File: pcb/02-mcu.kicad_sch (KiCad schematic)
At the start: 0 parts

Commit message: Setup project structure with organised sub-sheets
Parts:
- added U1: STM32G474RET6, Package_QFP:LQFP-64_10x10mm_P0.5mm, symbol MCU_ST_STM32G4:STM32G474RETx
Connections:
- new net: U1.15 (VSS), U1.31 (VSS), U1.47 (VSS), U1.63 (VSS)
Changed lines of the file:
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@@
 	(generator_version "10.0")
 	(paper "A4")
+	(symbol
+		(lib_id "MCU_ST_STM32G4:STM32G474RETx")
+		(at 59.69 71.12 0)
+		(unit 1)
+		(body_style 1)
+		(exclude_from_sim no)
+		(in_bom yes)
+		(on_board yes)
+		(in_pos_files yes)
+		(dnp no)
+		(fields_autoplaced yes)
+		(property "Reference" "U1"
+			(at 64.3733 119.38 0)
+			(show_name no)
+			(do_not_autoplace no)
+			(effects
+				(font
+					(size 1.27 1.27)
+				)
+				(justify left)
+			)
+		)
+		(property "Value" "STM32G474RET6"
+			(at 64.3733 121.92 0)
+			(show_name no)
+			(do_not_autoplace no)
+			(effects
+				(font
+					(size 1.27 1.27)
+				)
+				(justify left)
+			)
+		)
+		(property "Footprint" "Package_QFP:LQFP-64_10x10mm_P0.5mm"
+			(at 44.45 116.84 0)
+			(hide yes)
+			(show_name no)
+			(do_not_autoplace no)
+			(effects
+				(font
+					(size 1.27 1.27)
+				)
+				(justify right)
+			)
+		)
+		(property "Datasheet" "https://www.st.com/resource/en/datasheet/stm32g474re.pdf"
+			(at 59.69 71.12 0)
+			(hide yes)
+			(show_name no)
+			(do_not_autoplace no)
+			(effects
+				(font
+					(size 1.27 1.27)
+				)
+			)
+		)
+		(property "Description" "STMicroelectronics Arm Cortex-M4 MCU, 512KB flash, 128KB RAM, 170 MHz, 1.71-3.6V, 52 GPIO, LQFP64"
+			(at 59.69 71.12 0)
+			(hide yes)
+			(show_name no)
+			(do_not_autoplace no)
+			(effects
+				(font
+					(size 1.27 1.27)
+				)
+			)
+		)
+		(property "LCSC Part No" ""
+			(at 59.69 71.12 0)
+			(hide yes)
+			(show_name no)
+			(do_not_autoplace no)
+			(effects
+				(font
+					(size 1.27 1.27)
+				)
+			)
+		)
+		(property "Notes" ""
+			(at 59.69 71.12 0)
+			(hide yes)
+			(show_name no)
+			(do_not_autoplace no)
+			(effects
+				(font
+					(size 1.27 1.27)
+				)
+			)
+		)
+		(pin "40"
+		)
+		(pin "34"
+		)
+		(pin "36"
+		)
+		(pin "37"
+		)
+		(pin "38"
+		)
+		(pin "39"
+		)
+		(pin "35"
+		)
+		(pin "28"
+		)
+		(pin "30"
+		)
+		(pin "31"
+		)
+		(pin "32"
+		)
+		(pin "33"
+		)
+		(pin "29"
+		)
+		(pin "45"
+		)
+		(pin "46"
+		)
+		(pin "44"
+		)
+		(pin "47"
+		)
+		(pin "43"
+		)
+		(pin "48"
+		)
+		(pin "49"
+		)
+		(pin "42"
+		)
+		(pin "41"
+		)
+		(pin "1"
+		)
+		(pin "20"
+		)
+		(pin "19"
+		)
+		(pin "18"
+		)
+		(pin "17"
+		)
+		(pin "16"
+		)
+		(pin "15"
+		)
+		(pin "14"
+		)
+		(pin "13"
+		)
+		(pin "12"
+		)
+		(pin "11"
+		)
+		(pin "10"
+		)
+		(pin "9"
+		)
+		(pin "8"
+		)
+		(pin "7"
+		)
+		(pin "6"
+		)
+		(pin "5"
+		)
+		(pin "4"
+		)
+		(pin "3"
+		)
+		(pin "2"
+		)
+		(pin "50"
+		)
+		(pin "51"
+		)
+		(pin "52"
+		)
+		(pin "53"
+		)
+		(pin "54"
+		)
+		(pin "55"
+		)
+		(pin "56"
+		)
+		(pin "57"
+		)
+		(pin "58"
+		)
+		(pin "59"
+		)
+		(pin "60"
+		)
+		(pin "61"
+		)
+		(pin "62"
+		)
+		(pin "63"
+		)
+		(pin "64"
+		)
+		(pin "21"
+		)
+		(pin "27"
+		)
+		(pin "26"
+		)
+		(pin "25"
+		)
+		(pin "23"
+		)
+		(pin "22"
+		)
+		(pin "24"
+		)
+		(instances
+			(project "FluxNode-FOC"
+				(path "/c3755418-04f3-4b36-86ed-bd05a53b8f5f/2366da82-dc31-4919-b23c-1b211a77679f"
+					(reference "U1")
+					(unit 1)
+				)
+			)
+		)
+	)
 )

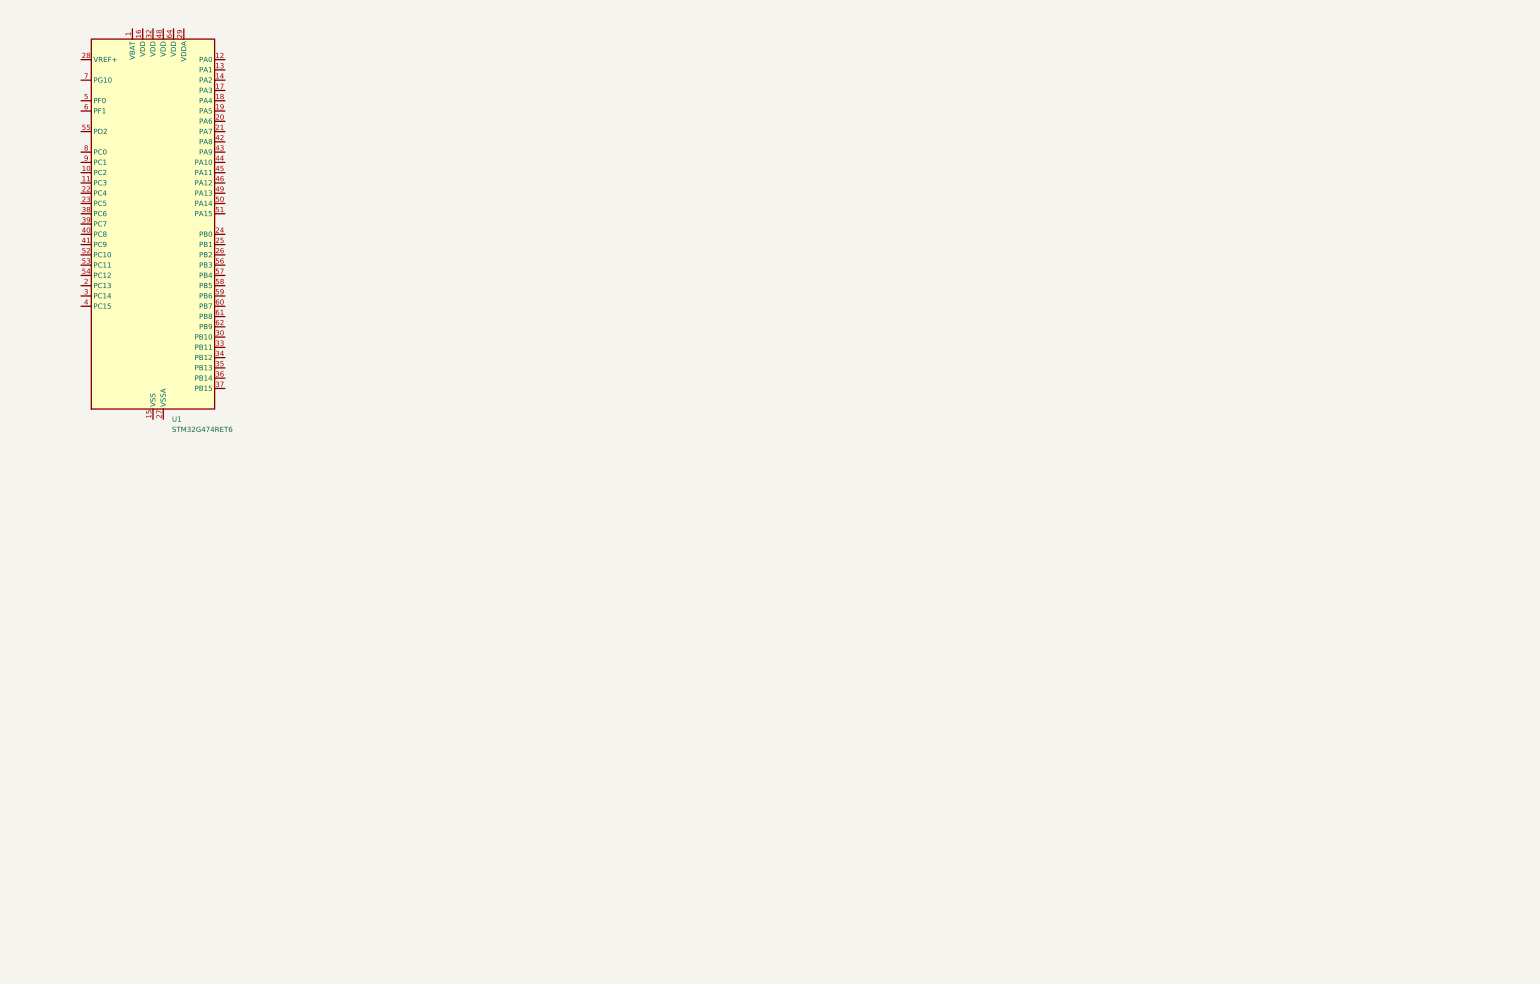
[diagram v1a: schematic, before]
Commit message: Planned MCU pinout and wired it to the gate driver
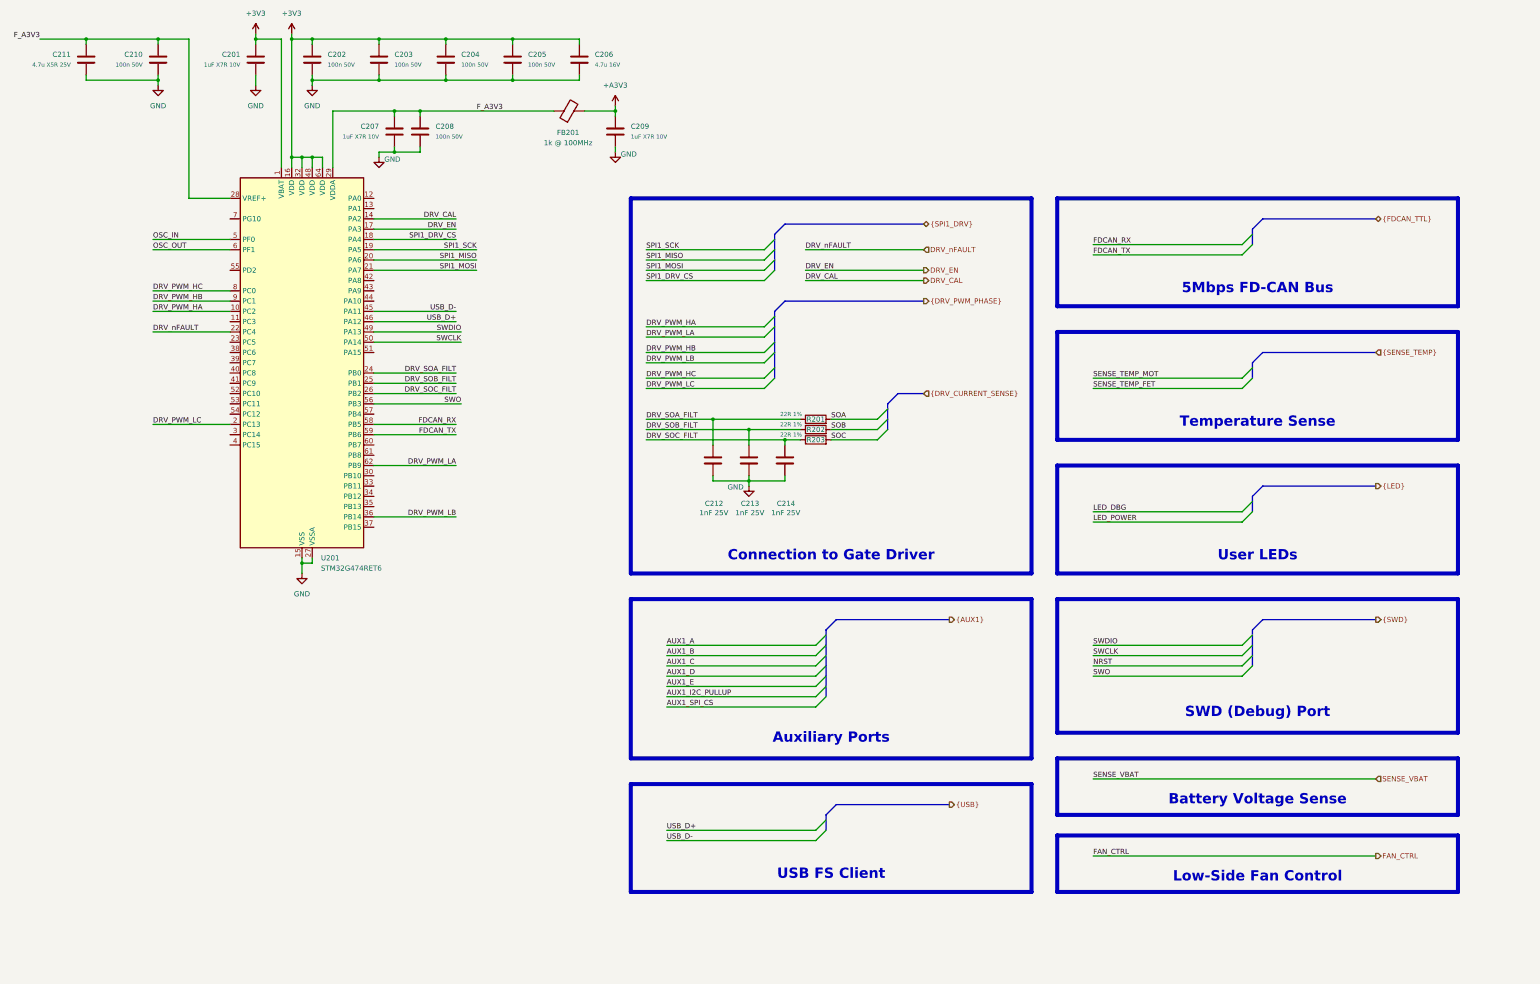
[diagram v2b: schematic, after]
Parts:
- added C201, C207, C209: 1uF X7R 10V, FluxNode-FOC:C_0402_1005_DensityHigh, symbol Device:C
- added C202, C203, C204, C205, C208, C210: 100n 50V, FluxNode-FOC:C_0402_1005_DensityHigh, symbol Device:C
- added C206: 4.7u 16V, FluxNode-FOC:C_0603_1608_DensityHigh, symbol Device:C
- added C211: 4.7u X5R 25V, FluxNode-FOC:C_0402_1005_DensityHigh, symbol Device:C
- added C212, C213, C214: 1nF 25V, symbol Device:C
- added FB201: 1k @ 100MHz, FluxNode-FOC:R_0805_2012_DensityHigh, symbol Device:FerriteBead
- added R201, R202, R203: 22R 1%, symbol Device:R
- renumbered U1 to U201
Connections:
- net +3V3: now reaches U201.1 (VBAT)
- net +3V3: now also U201.16 (VDD), U201.32 (VDD), U201.48 (VDD), U201.64 (VDD), C201.1, C202.1, C203.1, C204.1, C205.1, C206.1
- net DRV_PWM_HA: now reaches U201.10 (PC2)
- net DRV_CAL: now reaches U201.14 (PA2)
- net GND: now reaches U201.15 (VSS), U201.31 (VSS), U201.47 (VSS), U201.63 (VSS)
- net GND: now also U201.27 (VSSA), C201.2, C202.2, C203.2, C204.2, C205.2, C206.2, C207.2, C208.2, C209.2, C210.2, C211.2, C212.2, C213.2, C214.2
- net DRV_EN: now reaches U201.17 (PA3)
- net SPI1_DRV_CS: now reaches U201.18 (PA4)
- net SPI1_SCK: now reaches U201.19 (PA5)
- net DRV_PWM_LC: now reaches U201.2 (PC13)
- net SPI1_MISO: now reaches U201.20 (PA6)
- net SPI1_MOSI: now reaches U201.21 (PA7)
- net DRV_nFAULT: now reaches U201.22 (PC4)
- net DRV_SOA_FILT: now reaches U201.24 (PB0)
- net DRV_SOA_FILT: now also C212.1, R201.1
- net DRV_SOB_FILT: now reaches U201.25 (PB1)
- net DRV_SOB_FILT: now also C213.1, R202.1
- net DRV_SOC_FILT: now reaches U201.26 (PB2)
- net DRV_SOC_FILT: now also C214.1, R203.1
- net F_A3V3: now reaches U201.28 (VREF+)
- net F_A3V3: now also U201.29 (VDDA), C207.1, C208.1, C210.1, C211.1, FB201.1
- net DRV_PWM_LB: now reaches U201.36 (PB14)
- net USB_D-: now reaches U201.45 (PA11)
- net USB_D+: now reaches U201.46 (PA12)
- net SWDIO: now reaches U201.49 (PA13)
- net OSC_IN: now reaches U201.5 (PF0)
- net SWCLK: now reaches U201.50 (PA14)
- net SWO: now reaches U201.56 (PB3)
- net FDCAN_RX: now reaches U201.58 (PB5)
- net FDCAN_TX: now reaches U201.59 (PB6)
- net OSC_OUT: now reaches U201.6 (PF1)
- net DRV_PWM_LA: now reaches U201.62 (PB9)
- net DRV_PWM_HC: now reaches U201.8 (PC0)
- net DRV_PWM_HB: now reaches U201.9 (PC1)
- new net +A3V3: C209.1, FB201.2
- new net SOA: R201.2
- new net SOB: R202.2
- new net SOC: R203.2
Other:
- moved on the sheet: U201

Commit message: Ported CubeMX pinout to KiCad; Setup all the main busses to communicate with peripherals
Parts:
- added R204, R205: 22R 1%, FluxNode-FOC:R_0402_1005_DensityHigh, symbol Device:R
- C212, C213, C214: footprint (none) -> FluxNode-FOC:C_0402_1005_DensityHigh; Package (none) -> 0402
- R201, R202, R203: footprint (none) -> FluxNode-FOC:R_0402_1005_DensityHigh; Package (none) -> 0402
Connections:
- net FAN_CTRL: now also U201.33 (PB11)
- net NRST: now also U201.7 (PG10)
- net SENSE_TEMP_FET: now also U201.42 (PA8)
- net SENSE_TEMP_MOT: now also U201.43 (PA9)
- net SENSE_VBAT: now also U201.35 (PB13)
- net USB_D+: now also R204.1
- net USB_D-: now also R205.1
- net SENSE_TEMP_BRAKE: now reaches U201.34 (PB12)
- net USB_VBUS_SENSE: now reaches U201.37 (PB15)
- net BRAKE_PWM: now reaches U201.41 (PC9)
- net SPI3_SCK: now reaches U201.52 (PC10)
- net SPI3_MISO: now reaches U201.53 (PC11)
- net SPI3_MOSI: now reaches U201.54 (PC12)
- net AUX1_I2C_SDA: now reaches U201.60 (PB7)
- net AUX1_I2C_SCL: now reaches U201.61 (PB8)
- net SPI1_MISO renamed AUX1_SPI1_MISO
- net SPI1_MOSI renamed AUX1_SPI1_MOSI
- net SPI1_SCK renamed AUX1_SPI1_CLK

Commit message: Unified all different LCSC part numbers of the same exact components to just one variant
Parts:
- added C215, C216, C217: 470pF 50V, FluxNode-FOC:C_0402_1005_DensityHigh, symbol Device:C
- added R206, R207, R208: 1K 1%, FluxNode-FOC:R_0402_1005_DensityHigh, symbol Device:R
- C201, C207, C209: value 1uF X7R 10V -> 1uF 10V
- C202, C203, C204, C205, C208, C210: value 100n 50V -> 100nF 50V; LCSC C2649549 -> C361198; MPN GCM155R71H104KE02J -> C1005X7R1H104KT000F
- C211: value 4.7u X5R 25V -> 4.7u 25V
- C212, C213, C214: LCSC (none) -> C541372; MPN (none) -> CC0402KRX7R8BB102; Package 0402 -> (none)
- R201, R202, R203, R204, R205: LCSC (none) -> C482106; MPN (none) -> CRCW040222R0FKED; Package 0402 -> (none)
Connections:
- net GND: now also C215.2, C216.2, C217.2
- net SENSE_UA: now reaches U201.11 (PC3)
- net SENSE_UA: now also C215.1, R206.1
- net SENSE_UC: now reaches U201.12 (PA0)
- net SENSE_UC: now also C217.1, R208.1
- net SENSE_UB: now reaches U201.13 (PA1)
- net SENSE_UB: now also C216.1, R207.1
- net SPI1_MAG_CS: now reaches U201.23 (PC5)
- net AUX1_SPI1_CLK renamed SPI1_SCK
- net AUX1_SPI1_MISO renamed SPI1_MISO
- net AUX1_SPI1_MOSI renamed SPI1_MOSI
- net BRAKE_PWM renamed BRAKE_CTRL
- net SPI3_MISO renamed AUX1_SPI3_MISO
- net SPI3_MOSI renamed AUX1_SPI3_MOSI
- net SPI3_SCK renamed AUX1_SPI3_CLK
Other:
- company: (none) -> PhiMai
- moved on the sheet: C212, R201
